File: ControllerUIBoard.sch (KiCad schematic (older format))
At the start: 24 parts, among them J10 UIBoardCON1, J11 SignalStrength, J9 ATMEGA_PROG, SW1 KeySwitch, U15 ATmega4809-A

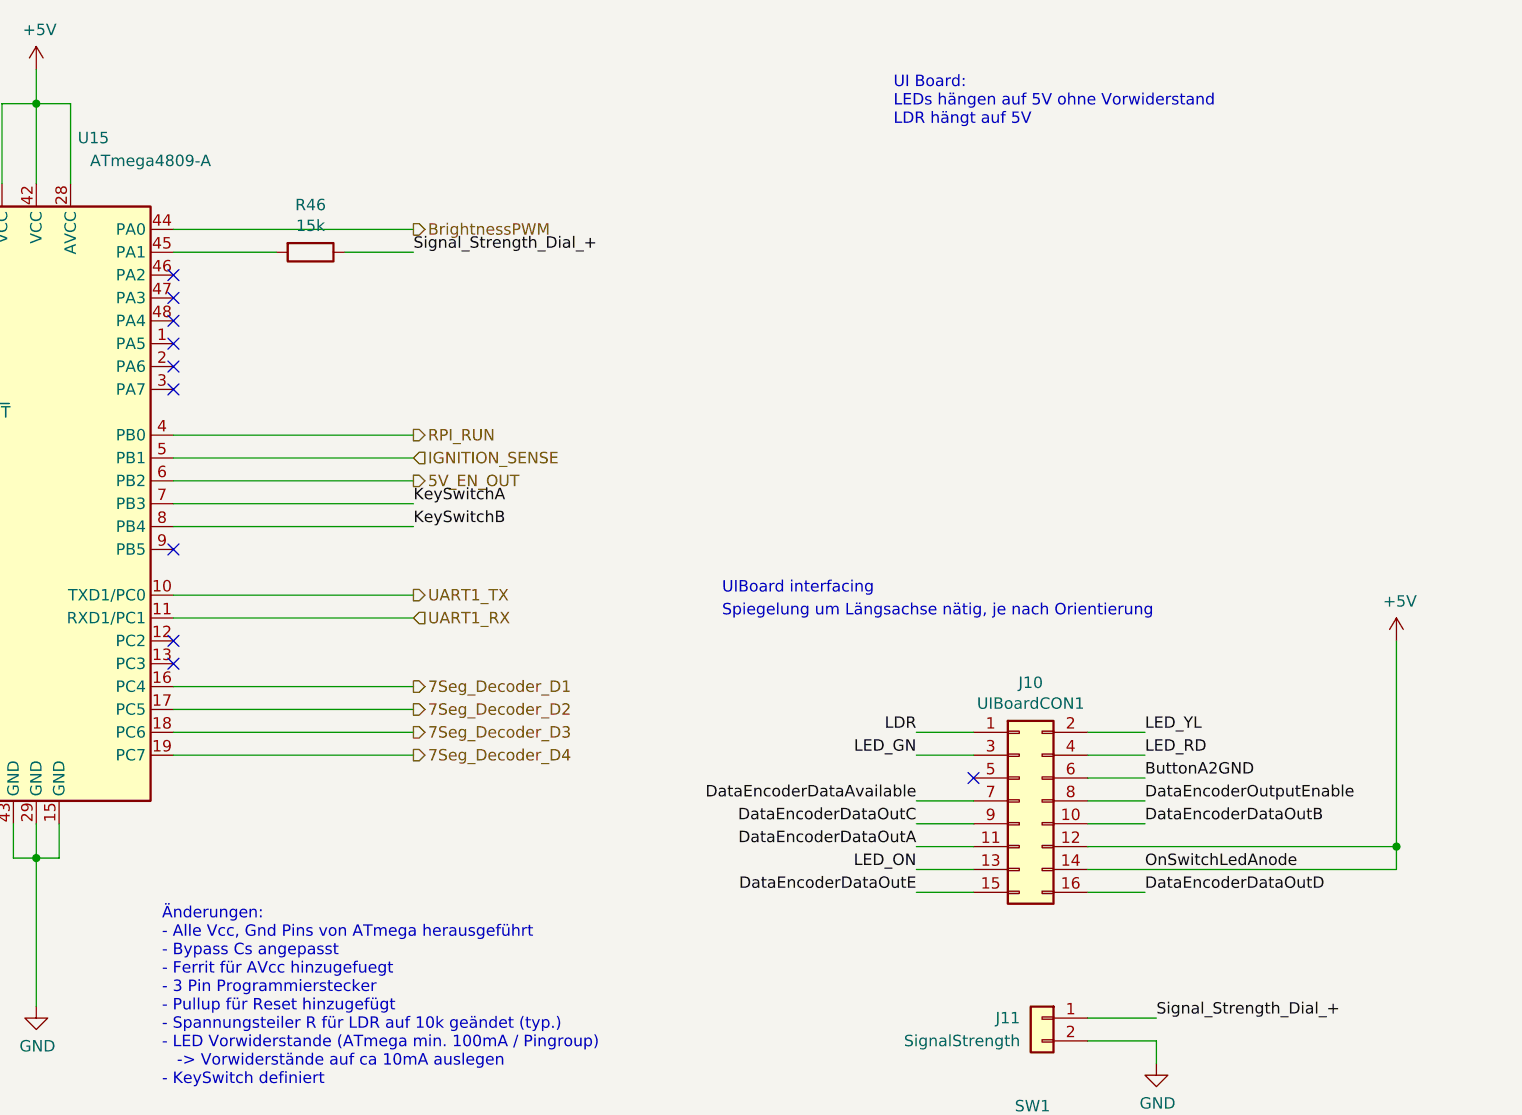
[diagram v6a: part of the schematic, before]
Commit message: - UI Backlight schaltbar gemacht, erster Entwurf, +5VA Symbol durch Label ersetzt
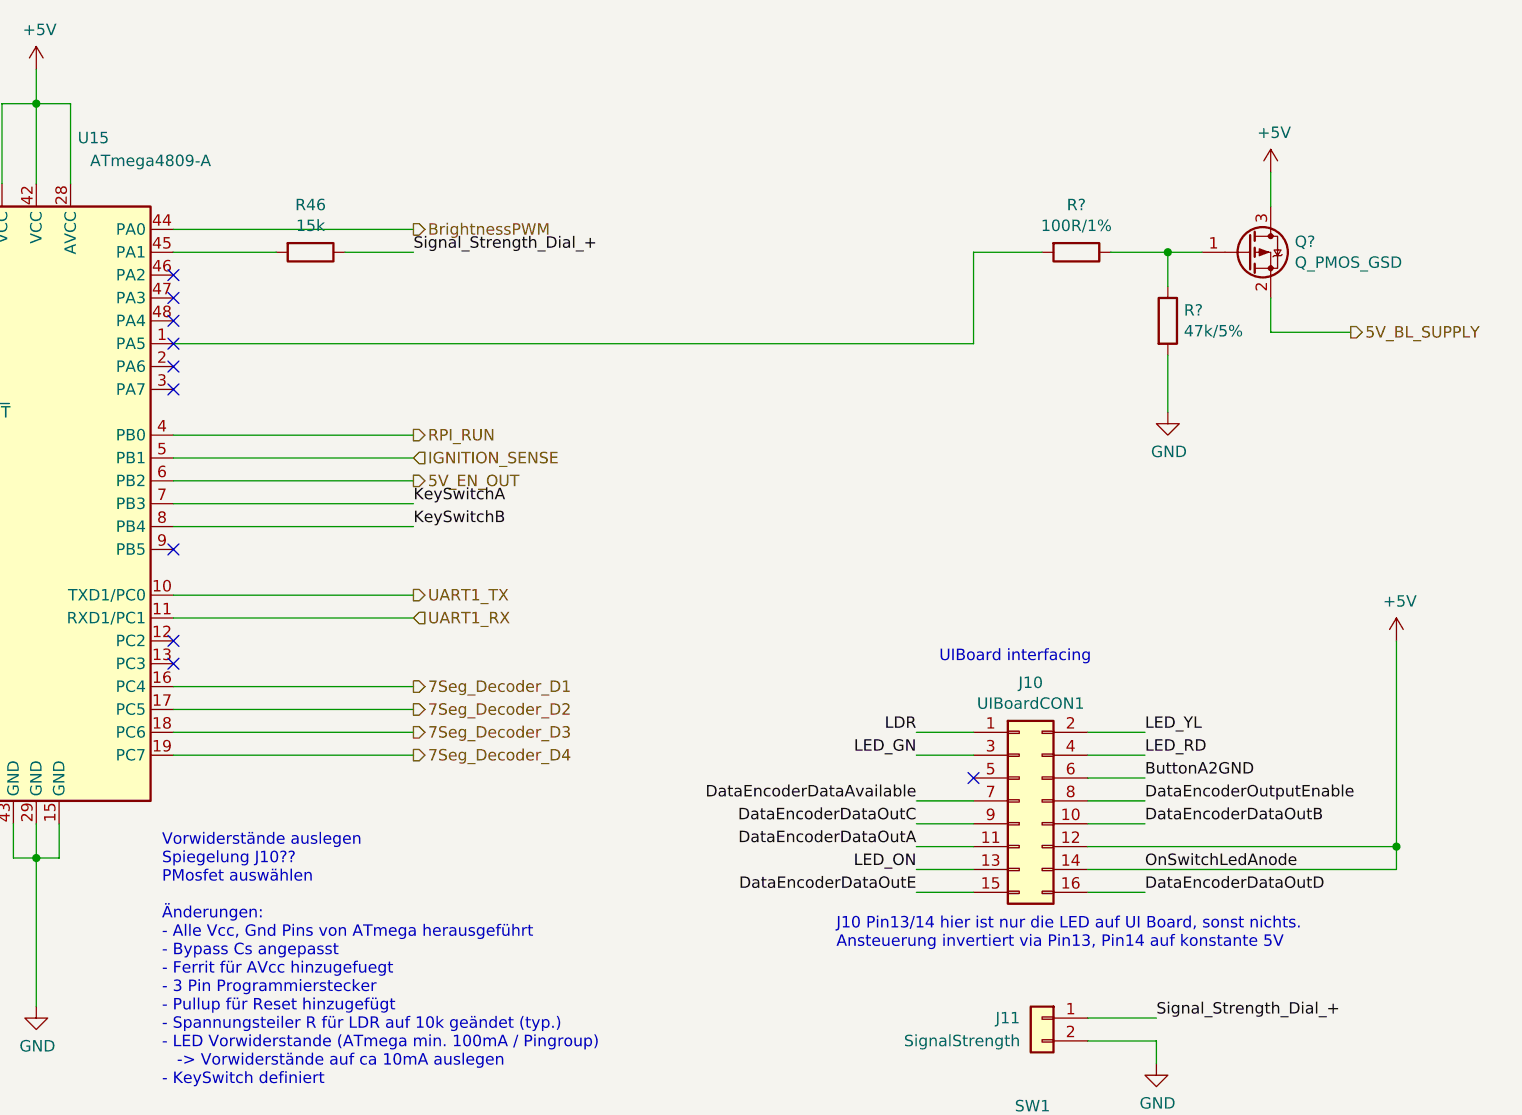
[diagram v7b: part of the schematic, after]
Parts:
- added Q?: Q_PMOS_GSD, symbol Device:Q_PMOS_GSD
- added R?: 47k/5%, Resistor_SMD:R_0402_1005Metric, symbol Device:R
- added R?: 100R/1%, Resistor_SMD:R_0402_1005Metric, symbol Device:R
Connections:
- net +5V: now also Q?.3 (D)
- net GND: now also R?.2
- net at U15.1 (PA5): now also R?.2
- new net: Q?.1 (G), R?.1, R?.1
- new net 5V_BL_SUPPLY: Q?.2 (S)
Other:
- note added: "J10 Pin13/14 hier ist nur die LED auf UI Board, sonst nichts.\nAnsteuerung invertiert via Pin13, Pin14 auf konstante 5V"
- note added: "Vorwiderstände auslegen\nSpiegelung J10??\nPMosfet auswählen\n\nÄnderungen:\n- Alle Vcc, Gnd Pins von ATmega herausgeführt\n- Bypass Cs angepasst\n- Ferrit für AVcc hinzugefuegt\n- 3 Pin Programmierstecker\n- Pullup für Reset hinzugefügt\n- Spannungsteiler R für LDR auf 10k geändet (typ.)\n- LED Vorwiderstande (ATmega min. 100mA / Pingroup)\n -> Vorwiderstände auf ca 10mA auslegen\n- KeySwitch de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"
- note removed: "Spiegelung um Längsachse nätig, je nach Orientierung"
- note removed: "UI Board:\nLEDs hängen auf 5V ohne Vorwiderstand\nLDR hängt auf 5V"
- note removed: "\n\nÄnderungen:\n- Alle Vcc, Gnd Pins von ATmega herausgeführt\n- Bypass Cs angepasst\n- Ferrit für AVcc hinzugefuegt\n- 3 Pin Programmierstecker\n- Pullup für Reset hinzugefügt\n- Spannungsteiler R für LDR auf 10k geändet (typ.)\n- LED Vorwiderstande (ATmega min. 100mA / Pingroup)\n -> Vorwiderstände auf ca 10mA auslegen\n- KeySwitch definiert"

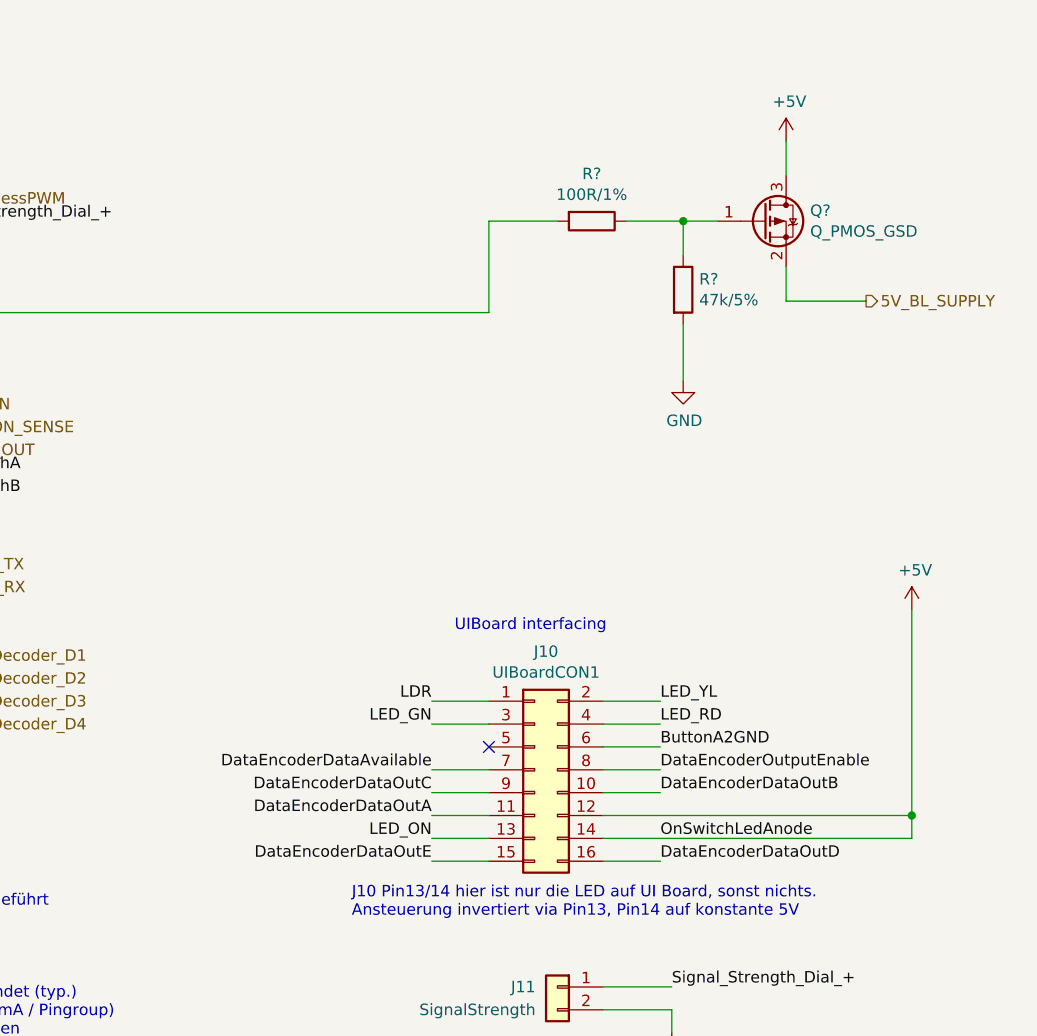
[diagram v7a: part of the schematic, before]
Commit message: [mod:] socket pin mirroring
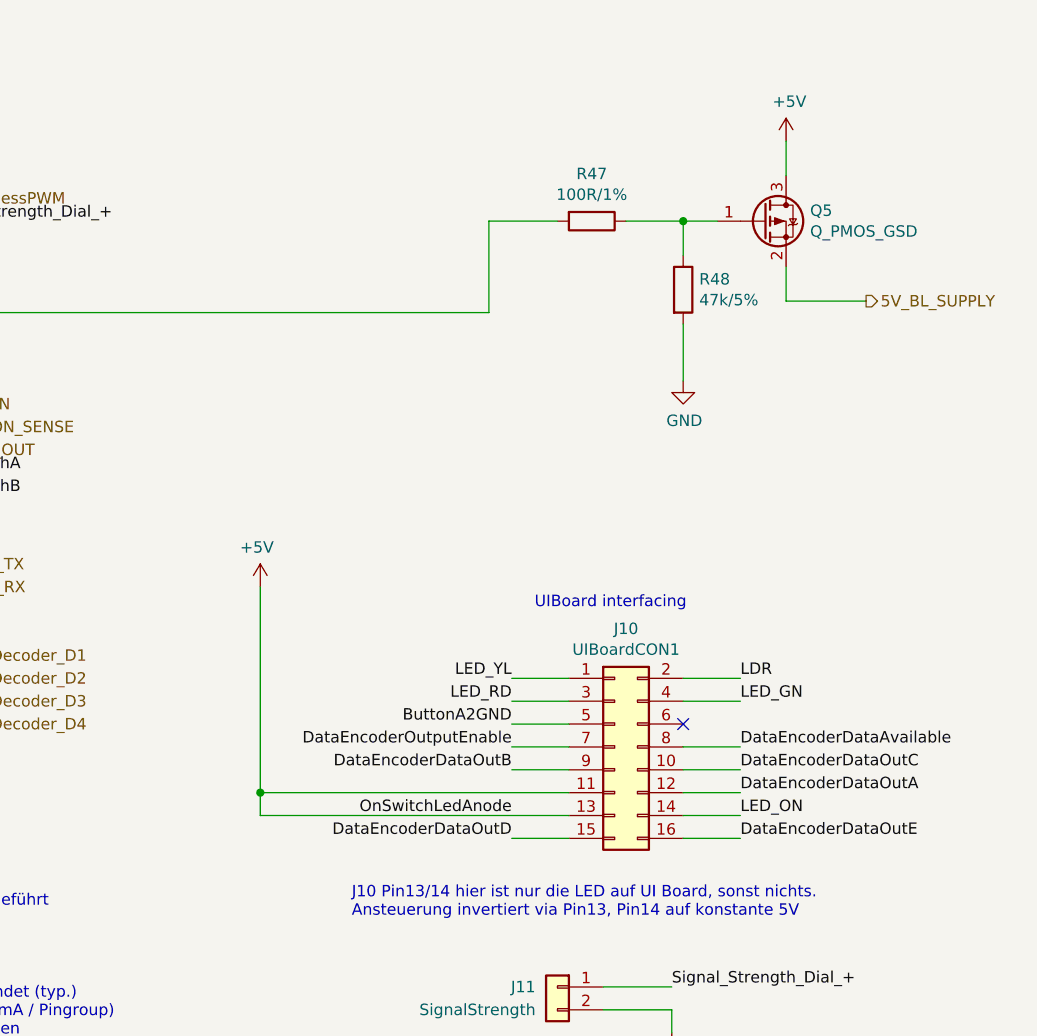
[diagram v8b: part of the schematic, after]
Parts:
- gave numbers to parts that had none: 3
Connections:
- net +5V: now also J10.11 (Pin_11), J10.13 (Pin_13); no longer J10.12 (Pin_12), J10.14 (Pin_14)
- net ButtonA2GND: now also J10.5 (Pin_5); no longer J10.6 (Pin_6)
- net DataEncoderDataAvailable: now also J10.8 (Pin_8); no longer J10.7 (Pin_7)
- net DataEncoderDataOutA: now also J10.12 (Pin_12); no longer J10.11 (Pin_11)
- net DataEncoderDataOutB: now also J10.9 (Pin_9); no longer J10.10 (Pin_10)
- net DataEncoderDataOutC: now also J10.10 (Pin_10); no longer J10.9 (Pin_9)
- net DataEncoderDataOutD: now also J10.15 (Pin_15); no longer J10.16 (Pin_16)
- net DataEncoderDataOutE: now also J10.16 (Pin_16); no longer J10.15 (Pin_15)
- net DataEncoderOutputEnable: now also J10.7 (Pin_7); no longer J10.8 (Pin_8)
- net LDR: now also J10.2 (Pin_2); no longer J10.1 (Pin_1)
- net LED_GN: now also J10.4 (Pin_4); no longer J10.3 (Pin_3)
- net LED_ON: now also J10.14 (Pin_14); no longer J10.13 (Pin_13)
- net LED_RD: now also J10.3 (Pin_3); no longer J10.4 (Pin_4)
- net LED_YL: now also J10.1 (Pin_1); no longer J10.2 (Pin_2)
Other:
- moved on the sheet: J10
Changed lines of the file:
@@
 L Connector_Generic:Conn_02x08_Odd_Even J?
 U 1 1 6205CD91
-P 9000 4150
+P 9350 4050
 AR Path="/6205CD91" Ref="J?"  Part="1"
 AR Path="/60F87146/6205CD91" Ref="J?"  Part="1"
 AR Path="/60F18E7A/6205CD91" Ref="J10"  Part="1"
-F 0 "J10" H 9050 4667 50  0000 C CNN
-F 1 "UIBoardCON1" H 9050 4576 50  0000 C CNN
-F 2 "Connector_PinSocket_2.54mm:PinSocket_2x08_P2.54mm_Vertical" H 9000 4150 50  0001 C CNN
-F 3 "~" H 9000 4150 50  0001 C CNN
-	1    9000 4150
-	1    0    0    -1
-$EndComp
-Text Label 8550 4150 2    50   ~ 0
-DataEncoderDataAvailable
-Text Label 8550 4250 2    50   ~ 0
-DataEncoderDataOutC
-Text Label 8550 4350 2    50   ~ 0
-DataEncoderDataOutA
-Text Label 8550 4550 2    50   ~ 0
-DataEncoderDataOutE
-Text Label 9550 4550 0    50   ~ 0
+F 0 "J10" H 9400 4567 50  0000 C CNN
+F 1 "UIBoardCON1" H 9400 4476 50  0000 C CNN
+F 2 "Connector_PinSocket_2.54mm:PinSocket_2x08_P2.54mm_Vertical" H 9350 4050 50  0001 C CNN
+F 3 "~" H 9350 4050 50  0001 C CNN
+	1    9350 4050
+	1    0    0    -1
+$EndComp
+Text Label 8900 4450 2    50   ~ 0
 DataEncoderDataOutD
-Text Label 9550 4450 0    50   ~ 0
+Text Label 8900 4350 2    50   ~ 0
 OnSwitchLedAnode
-Text Label 9550 4250 0    50   ~ 0
+Text Label 8900 4150 2    50   ~ 0
 DataEncoderDataOutB
 Text Label 9600 5100 0    50   ~ 0
 Signal_Strength_Dial_+
-Text Label 8550 3850 2    50   ~ 0
-LDR
-Text Label 8550 3950 2    50   ~ 0
-LED_GN
-Text Label 9550 4150 0    50   ~ 0
+Text Label 8900 4050 2    50   ~ 0
 DataEncoderOutputEnable
-Text Label 9550 4050 0    50   ~ 0
+Text Label 8900 3950 2    50   ~ 0
 ButtonA2GND
-Text Label 9550 3950 0    50   ~ 0
+Text Label 8900 3850 2    50   ~ 0
 LED_RD
-Text Label 9550 3850 0    50   ~ 0
+Text Label 8900 3750 2    50   ~ 0
 LED_YL
 $Comp
 L power:+5V #PWR?
 U 1 1 6205CDAB
-P 10650 3450
+P 7800 3350
 AR Path="/6205CDAB" Ref="#PWR?"  Part="1"
 AR Path="/60F87146/6205CDAB" Ref="#PWR?"  Part="1"
 AR Path="/60F18E7A/6205CDAB" Ref="#PWR0189"  Part="1"
-F 0 "#PWR0189" H 10650 3300 50  0001 C CNN
-F 1 "+5V" H 10665 3623 50  0000 C CNN
-F 2 "" H 10650 3450 50  0001 C CNN
-F 3 "" H 10650 3450 50  0001 C CNN
-	1    10650 3450
-	1    0    0    -1
-$EndComp
-Wire Wire Line
-	10650 4350 10650 3450
-Text Notes 8650 3550 0    50   ~ 0
+F 0 "#PWR0189" H 7800 3200 50  0001 C CNN
+F 1 "+5V" H 7815 3523 50  0000 C CNN
+F 2 "" H 7800 3350 50  0001 C CNN
+F 3 "" H 7800 3350 50  0001 C CNN
+	1    7800 3350
+	-1   0    0    -1
+$EndComp
+Wire Wire Line
+	7800 4250 7800 3350
+Text Notes 9000 3450 0    50   ~ 0
 UIBoard interfacing\n
 Wire Wire Line
@@
 	9600 5950 9300 5950
 Wire Wire Line
-	8800 3850 8550 3850
-Wire Wire Line
-	8550 3950 8800 3950
-Wire Wire Line
-	8800 4150 8550 4150
-Wire Wire Line
-	8550 4250 8800 4250
-Wire Wire Line
-	8800 4350 8550 4350
-Wire Wire Line
-	8800 4550 8550 4550
-Wire Wire Line
-	9300 4550 9550 4550
-Wire Wire Line
-	9550 4250 9300 4250
-Wire Wire Line
-	9300 4150 9550 4150
-Wire Wire Line
-	9550 4050 9300 4050
-Wire Wire Line
-	9300 3950 9550 3950
-Wire Wire Line
-	9550 3850 9300 3850
-NoConn ~ 8800 4050
+	9650 3750 9900 3750
+Wire Wire Line
+	9900 3850 9650 3850
+Wire Wire Line
+	9650 4050 9900 4050
+Wire Wire Line
+	9900 4150 9650 4150
+Wire Wire Line
+	9650 4250 9900 4250
+Wire Wire Line
+	9650 4450 9900 4450
+Wire Wire Line
+	9150 4450 8900 4450
+Wire Wire Line
+	8900 4150 9150 4150
+Wire Wire Line
+	9150 4050 8900 4050
+Wire Wire Line
+	8900 3950 9150 3950
+Wire Wire Line
+	9150 3850 8900 3850
+Wire Wire Line
+	8900 3750 9150 3750
 Wire Wire Line
 	9300 5100 9600 5100
 Wire Wire Line
-	9300 4350 10650 4350
+	9150 4250 7800 4250
 $Comp
 L power:GND #PWR?
@@
 	1    0    0    -1
 $EndComp
-Text Label 8550 4450 2    50   ~ 0
-LED_ON
-Wire Wire Line
-	8550 4450 8800 4450
+Wire Wire Line
+	9900 4350 9650 4350
 Text Label 9600 5750 0    50   ~ 0
 KeySwitchA
@@
 J10 Pin13/14 hier ist nur die LED auf UI Board, sonst nichts.\nAnsteuerung invertiert via Pin13, Pin14 auf konstante 5V
 Wire Wire Line
-	10650 4450 10650 4350
-Wire Wire Line
-	9300 4450 10650 4450
-Connection ~ 10650 4350
-$Comp
-L Device:Q_PMOS_GSD Q?
+	7800 4350 7800 4250
+Wire Wire Line
+	9150 4350 7800 4350
+Connection ~ 7800 4250
+$Comp
+L Device:Q_PMOS_GSD Q5
 U 1 1 617E35E3
 P 10000 1750
-F 0 "Q?" H 10205 1796 50  0000 L CNN
+F 0 "Q5" H 10205 1796 50  0000 L CNN
 F 1 "Q_PMOS_GSD" H 10205 1705 50  0000 L CNN
 F 2 "" H 10200 1850 50  0001 C CNN
@@
 AR Path="/617EFAAD" Ref="#PWR?"  Part="1"
 AR Path="/60F87146/617EFAAD" Ref="#PWR?"  Part="1"
-AR Path="/60F18E7A/617EFAAD" Ref="#PWR?"  Part="1"
-F 0 "#PWR?" H 10100 1250 50  0001 C CNN
+AR Path="/60F18E7A/617EFAAD" Ref="#PWR0101"  Part="1"
+F 0 "#PWR0101" H 10100 1250 50  0001 C CNN
 F 1 "+5V" H 10115 1573 50  0000 C CNN
 F 2 "" H 10100 1400 50  0001 C CNN
@@
 $EndComp
 $Comp
-L Device:R R?
+L Device:R R48
 U 1 1 617F3C36
 P 9650 2050
-F 0 "R?" H 9720 2096 50  0000 L CNN
+F 0 "R48" H 9720 2096 50  0000 L CNN
 F 1 "47k/5%" H 9720 2005 50  0000 L CNN
 F 2 "Resistor_SMD:R_0402_1005Metric" V 9580 2050 50  0001 C CNN
@@
 AR Path="/617F448C" Ref="#PWR?"  Part="1"
 AR Path="/60F87146/617F448C" Ref="#PWR?"  Part="1"
-AR Path="/60F18E7A/617F448C" Ref="#PWR?"  Part="1"
-F 0 "#PWR?" H 9650 2200 50  0001 C CNN
+AR Path="/60F18E7A/617F448C" Ref="#PWR0190"  Part="1"
+F 0 "#PWR0190" H 9650 2200 50  0001 C CNN
 F 1 "GND" H 9655 2277 50  0000 C CNN
 F 2 "" H 9650 2450 50  0001 C CNN
@@
 	9650 2200 9650 2450
 $Comp
-L Device:R R?
+L Device:R R47
 U 1 1 61801558
 P 9250 1750
-F 0 "R?" V 9043 1750 50  0000 C CNN
+F 0 "R47" V 9043 1750 50  0000 C CNN
 F 1 "100R/1%" V 9134 1750 50  0000 C CNN
 F 2 "Resistor_SMD:R_0402_1005Metric" V 9180 1750 50  0001 C CNN
@@
 Text HLabel 10450 2100 2    50   Output ~ 0
 5V_BL_SUPPLY
+Text Label 9900 4350 0    50   ~ 0
+LED_ON
+Text Label 9900 3850 0    50   ~ 0
+LED_GN
+Text Label 9900 3750 0    50   ~ 0
+LDR
+Text Label 9900 4450 0    50   ~ 0
+DataEncoderDataOutE
+Text Label 9900 4250 0    50   ~ 0
+DataEncoderDataOutA
+Text Label 9900 4150 0    50   ~ 0
+DataEncoderDataOutC
+Text Label 9900 4050 0    50   ~ 0
+DataEncoderDataAvailable
+NoConn ~ 9650 3950
 $EndSCHEMATC
